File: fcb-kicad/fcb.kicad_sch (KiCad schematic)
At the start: 33 parts, among them Q1 S8050 J3Y, U1 TPS5430DDA, U2 AMS1117-3.3, U3 DL-RTS4432, U4 LSM6DS3, U5 STM32F411CEUx, U6 W25Q128JVS

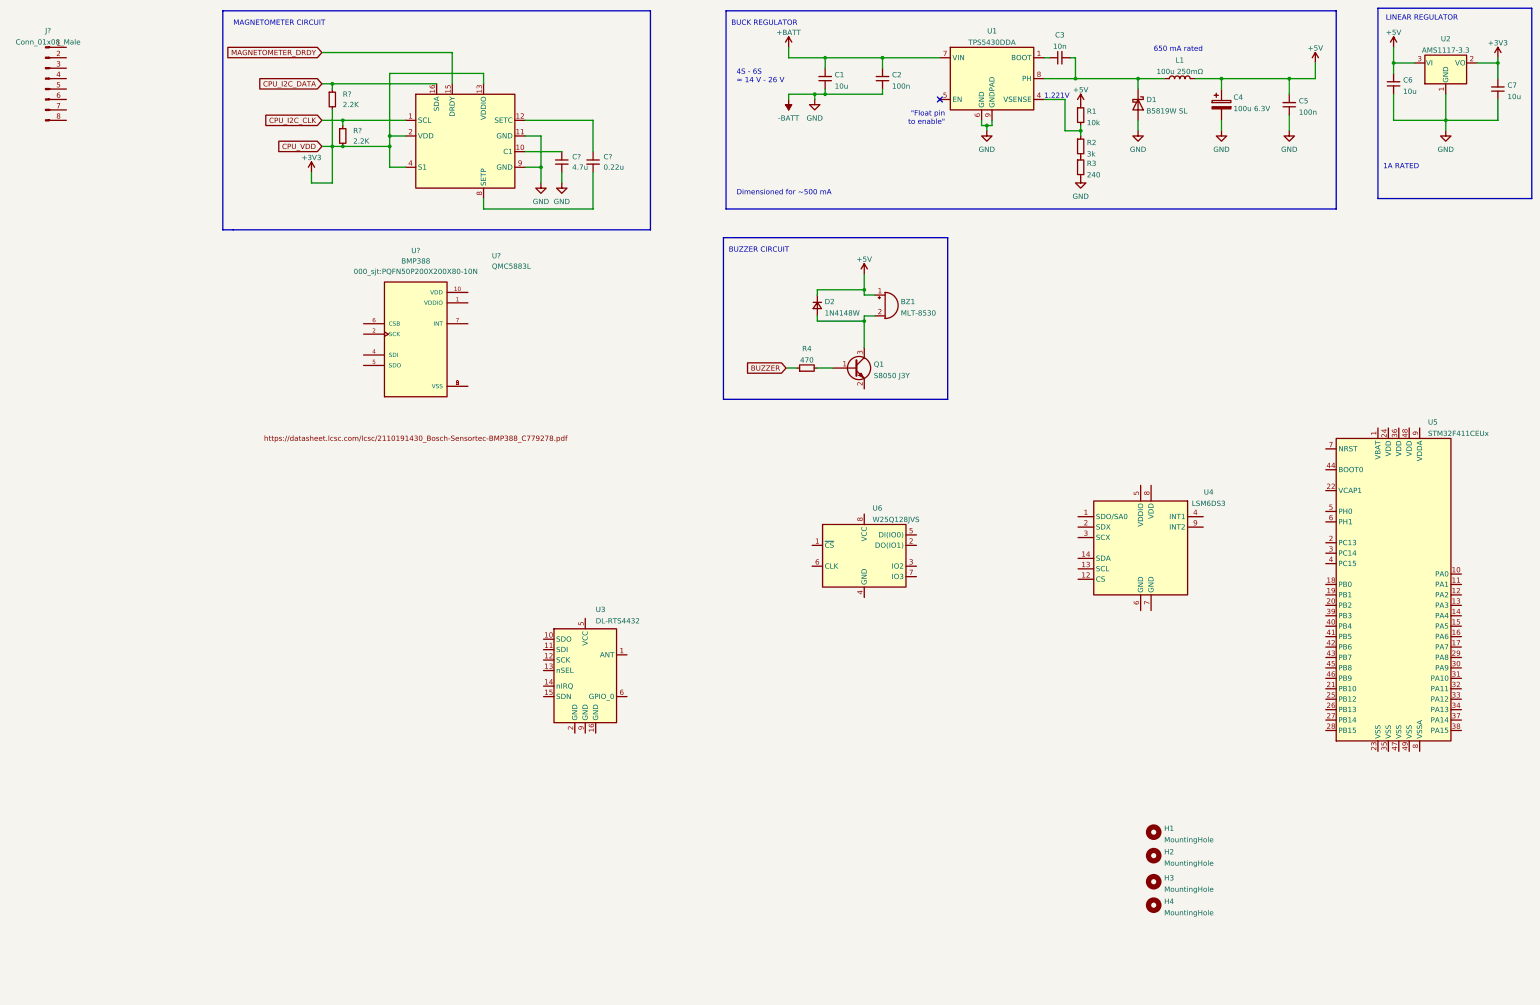
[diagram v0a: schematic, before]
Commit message: Added imu circuit
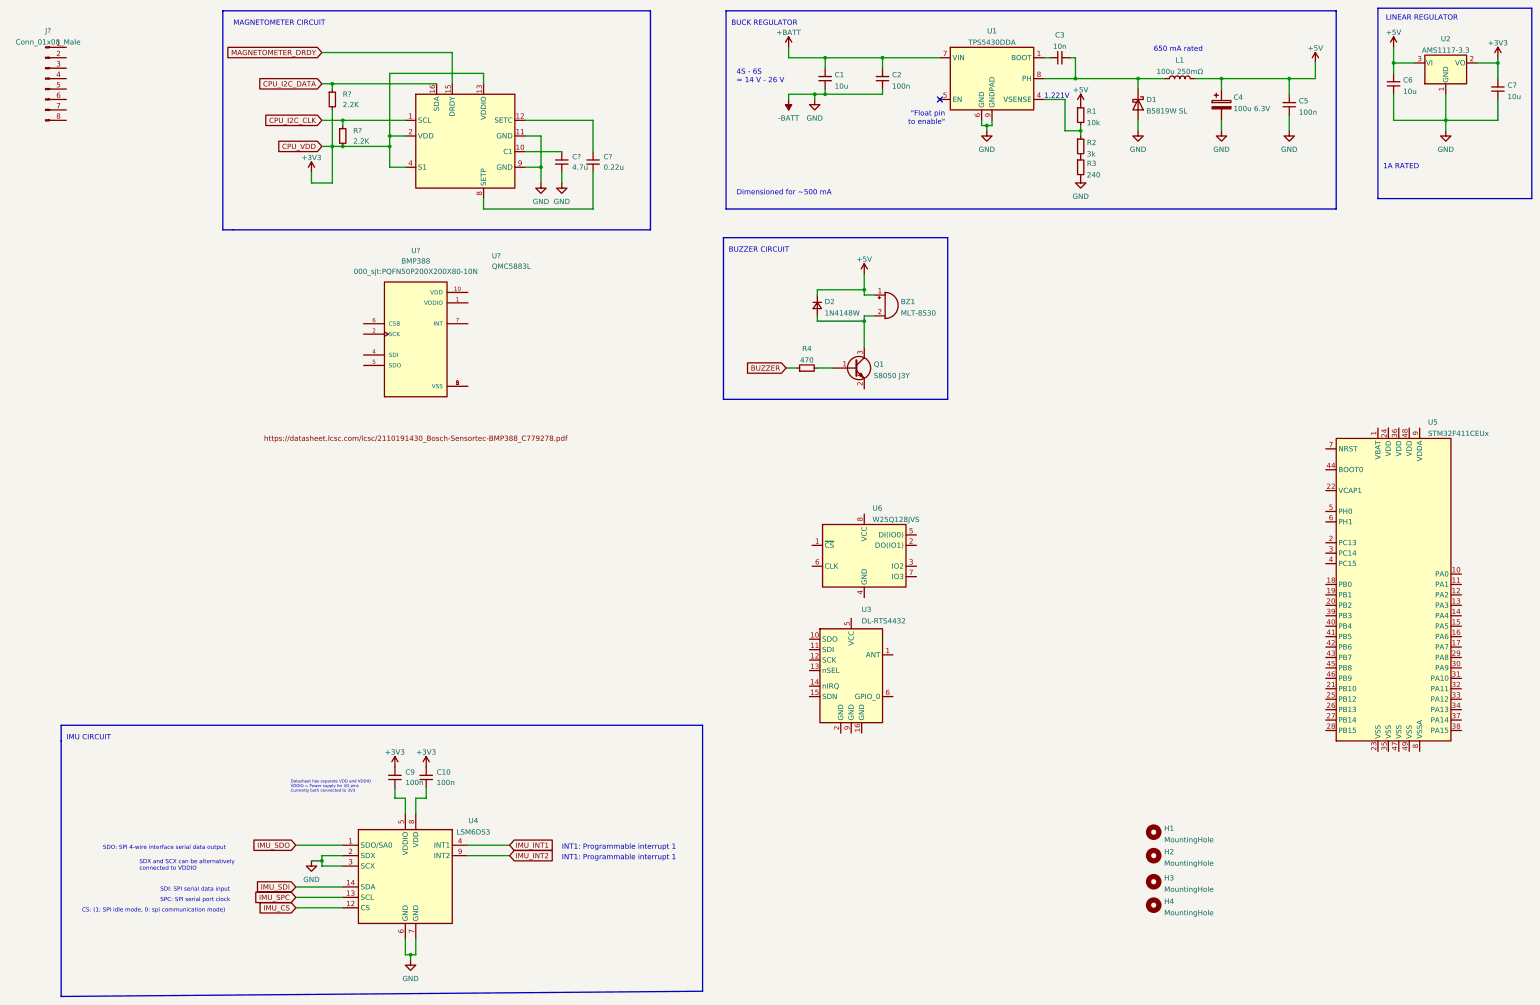
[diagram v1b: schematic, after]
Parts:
- added C10, C9: 100n, Capacitor_SMD:C_0603_1608Metric_Pad1.08x0.95mm_HandSolder, symbol Device:C_Small
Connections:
- net +3V3: now also C10.2, C9.2
- net -BATT: now also U4.2 (SDX), U4.3 (SCX), U4.6 (GND), U4.7 (GND)
- net IMU_SDO: now reaches U4.1 (SDO/SA0)
- net IMU_CS: now reaches U4.12 (CS)
- net IMU_SPC: now reaches U4.13 (SCL)
- net IMU_SDI: now reaches U4.14 (SDA)
- net IMU_INT1: now reaches U4.4 (INT1)
- net at U4.5 (VDDIO): now also C9.1
- net at U4.8 (VDD): now also C10.1
- net IMU_INT2: now reaches U4.9 (INT2)
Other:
- note added: "CS: (1: SPI idle mode, 0: spi communication mode)"
- note added: "Datasheet has separate VDD and VDDIO VDDIO = Power supply for I/O pins Currently both connected to 3V3"
- note added: "IMU CIRCUIT"
- note added: "INT1: Programmable interrupt 1"
- note added: "SDI: SPI serial data input"
- note added: "SDO: SPI 4-wire interface serial data output"
- note added: "SDX and SCX can be alternatively connected to VDDIO"
- note added: "SPC: SPI serial port clock"
- moved on the sheet: U3, U4

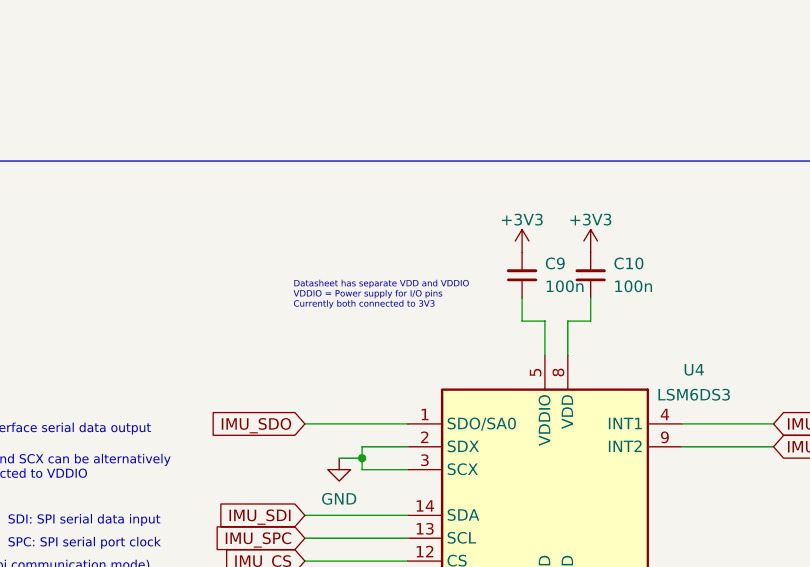
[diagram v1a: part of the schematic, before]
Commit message: Added imu circuit
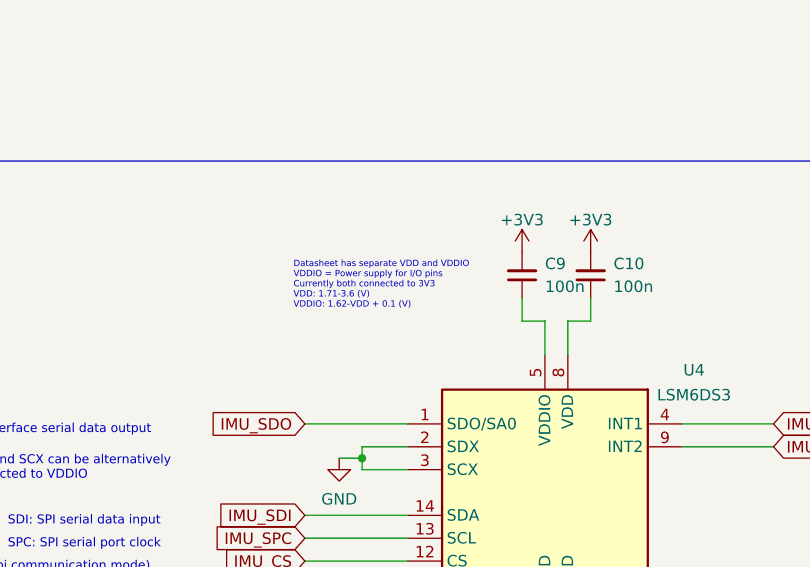
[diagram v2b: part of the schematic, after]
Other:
- note added: "Datasheet has separate VDD and VDDIO VDDIO = Power supply for I/O pins Currently both connected to 3V3 VDD: 1.71-3.6 (V) VDDIO: 1.62-VDD + 0.1 (V)"
- note removed: "Datasheet has separate VDD and VDDIO VDDIO = Power supply for I/O pins Currently both connected to 3V3"
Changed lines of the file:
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@@
     (effects (font (size 1 1)) (justify left bottom))
   )
-  (text "Datasheet has separate VDD and VDDIO \nVDDIO = Power supply for I/O pins\nCurrently both connected to 3V3"
+  (text "Datasheet has separate VDD and VDDIO \nVDDIO = Power supply for I/O pins\nCurrently both connected to 3V3\nVDD: 1.71-3.6 (V)\nVDDIO: 1.62-VDD + 0.1 (V)"
     (at 90.17 212.09 0)
     (effects (font (size 0.7 0.7)) (justify left bottom))
